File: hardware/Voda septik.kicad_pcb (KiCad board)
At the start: 2 copper layers, 1 part, among them U1 ESP32-DevKitC-30

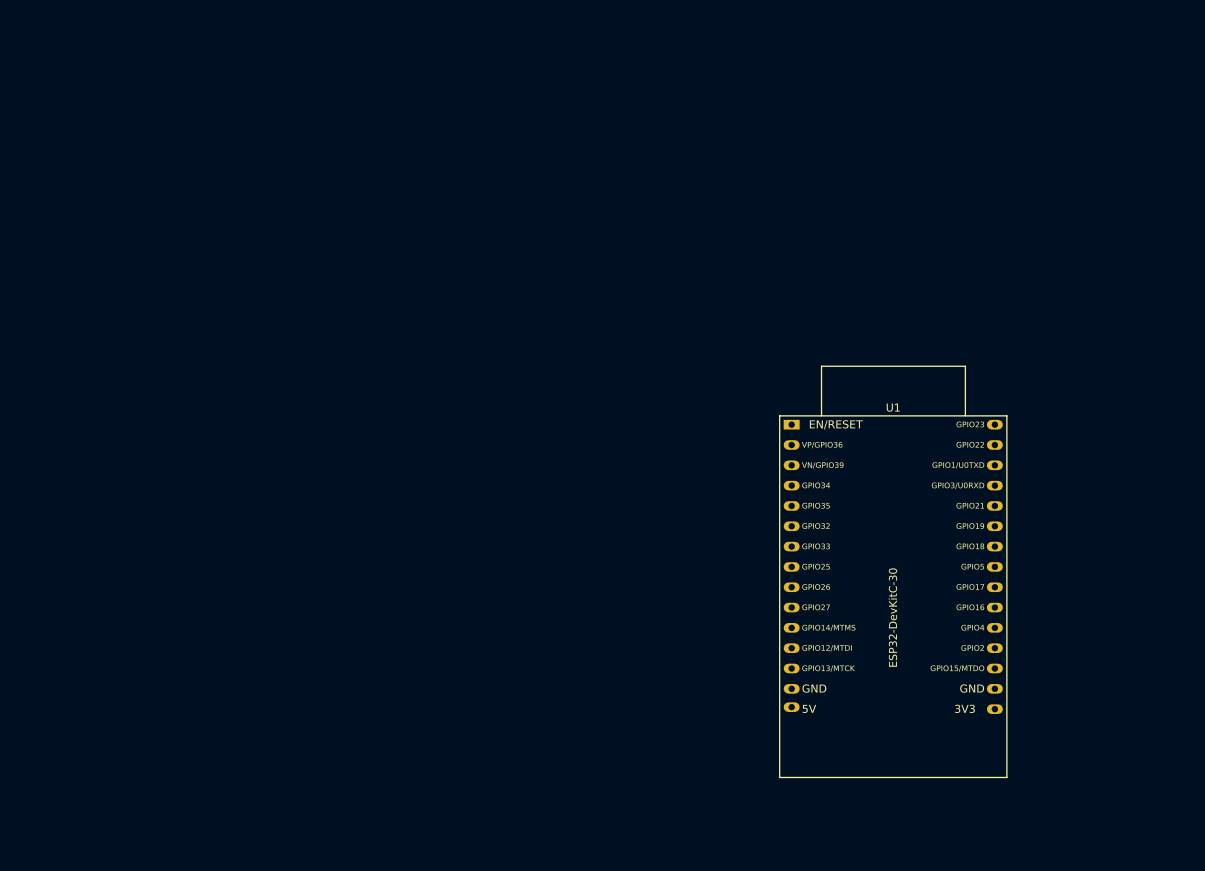
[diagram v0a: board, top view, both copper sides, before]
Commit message: Vyvéjíme PCB a jsme v v koncích díky malé krabičce.
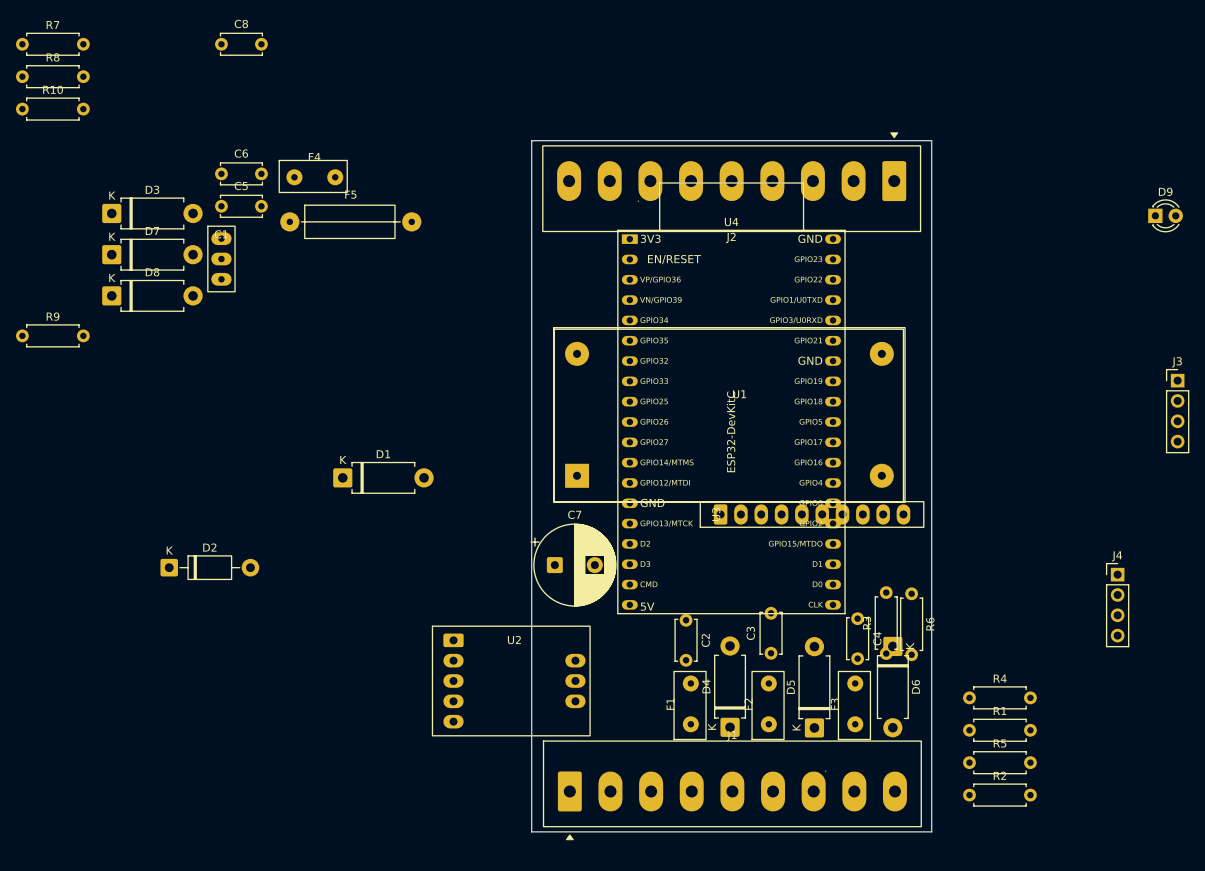
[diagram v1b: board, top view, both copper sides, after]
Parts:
- added C1: 100n, martin:Odruseni_3x_2.54mm, F.Cu at (53.2, 67.8)
- added C2: 100n, Capacitor_THT:C_Disc_D5.0mm_W2.5mm_P5.00mm, F.Cu at (111.3, 115.5)
- added C3: 100n, Capacitor_THT:C_Disc_D5.0mm_W2.5mm_P5.00mm, F.Cu at (121.9, 119.6)
- added C4: 100n, Capacitor_THT:C_Disc_D5.0mm_W2.5mm_P5.00mm, F.Cu at (132.7, 115.2)
- added C5: 1n, Capacitor_THT:C_Disc_D5.0mm_W2.5mm_P5.00mm, F.Cu at (53.2, 63.7)
- added C6: 100p, Capacitor_THT:C_Disc_D5.0mm_W2.5mm_P5.00mm, F.Cu at (53.2, 59.6)
- added C7: 470u, Capacitor_THT:CP_Radial_D10.0mm_P5.00mm, F.Cu at (94.9, 108.5)
- added C8: 100n, Capacitor_THT:C_Disc_D5.0mm_W2.5mm_P5.00mm, F.Cu at (53.2, 43.5)
- added D1: BZW04-5V8, Diode_THT:D_DO-15_P10.16mm_Horizontal, F.Cu at (68.4, 97.7)
- added D2: 1N4007, Diode_THT:D_DO-41_SOD81_P10.16mm_Horizontal, F.Cu at (46.7, 108.9)
- added D3: BZW06-26, Diode_THT:D_DO-15_P10.16mm_Horizontal, F.Cu at (39.5, 64.6)
- added D4: BZW04-5V8, Diode_THT:D_DO-15_P10.16mm_Horizontal, F.Cu at (116.8, 128.8)
- added D5: BZW04-5V8, Diode_THT:D_DO-15_P10.16mm_Horizontal, F.Cu at (127.3, 128.9)
- added D6: BZW04-5V8, Diode_THT:D_DO-15_P10.16mm_Horizontal, F.Cu at (137.1, 118.7)
- added D7: BZW04-5V8, Diode_THT:D_DO-15_P10.16mm_Horizontal, F.Cu at (39.5, 69.8)
- added D8: BZW04-5V8, Diode_THT:D_DO-15_P10.16mm_Horizontal, F.Cu at (39.5, 74.9)
- added D9: LED, LED_THT:LED_D3.0mm, F.Cu at (170.0, 64.9)
- added F1: 50mA, martin:Fuse_Disc_D8.3_W3.8_P5.1, F.Cu at (111.9, 128.4)
- added F2: 50mA, martin:Fuse_Disc_D8.3_W3.8_P5.1, F.Cu at (121.6, 128.4)
- added F3: 50mA, martin:Fuse_Disc_D8.3_W3.8_P5.1, F.Cu at (132.4, 128.4)
- added F4: 50mA, martin:Fuse_Disc_D8.3_W3.8_P5.1, F.Cu at (62.3, 60.1)
- added F5: 0,5A, martin:Fuse_Axial_L11mm_D3.9mm_P15.24mm_Horizontal, F.Cu at (61.8, 65.7)
- added J1: Screw_Terminal_01x09, martin:Svorky_EB147A_9_5.08, F.Cu at (96.8, 136.8)
- added J2: Screw_Terminal_01x09, martin:Svorky_EB147A_9_5.08, F.Cu at (137.3, 60.5)
- added J3: Display LCD I2C, Connector_PinHeader_2.54mm:PinHeader_1x04_P2.54mm_Vertical, F.Cu at (172.7, 85.5)
- added J4: Display TM1637, Connector_PinHeader_2.54mm:PinHeader_1x04_P2.54mm_Vertical, F.Cu at (165.2, 109.7)
- added R1: 100R, Resistor_THT:R_Axial_DIN0207_L6.3mm_D2.5mm_P7.62mm_Horizontal, F.Cu at (146.7, 129.2)
- added R10: 330R, Resistor_THT:R_Axial_DIN0207_L6.3mm_D2.5mm_P7.62mm_Horizontal, F.Cu at (28.3, 51.5)
- added R2: 100R, Resistor_THT:R_Axial_DIN0207_L6.3mm_D2.5mm_P7.62mm_Horizontal, F.Cu at (146.7, 137.3)
- added R3: 100R, Resistor_THT:R_Axial_DIN0207_L6.3mm_D2.5mm_P7.62mm_Horizontal, F.Cu at (136.3, 119.6)
- added R4: 2k2, Resistor_THT:R_Axial_DIN0207_L6.3mm_D2.5mm_P7.62mm_Horizontal, F.Cu at (146.7, 125.2)
- added R5: 2k2, Resistor_THT:R_Axial_DIN0207_L6.3mm_D2.5mm_P7.62mm_Horizontal, F.Cu at (146.7, 133.2)
- added R6: 2k2, Resistor_THT:R_Axial_DIN0207_L6.3mm_D2.5mm_P7.62mm_Horizontal, F.Cu at (139.5, 112.1)
- added R7: 2k2, Resistor_THT:R_Axial_DIN0207_L6.3mm_D2.5mm_P7.62mm_Horizontal, F.Cu at (28.3, 43.5)
- added R8: 3k9, Resistor_THT:R_Axial_DIN0207_L6.3mm_D2.5mm_P7.62mm_Horizontal, F.Cu at (28.3, 47.5)
- added R9: 56R, Resistor_THT:R_Axial_DIN0207_L6.3mm_D2.5mm_P7.62mm_Horizontal, F.Cu at (28.3, 79.9)
- added U1: DC-DC 24V -> 5V, martin:LM2596 DC-DC HW-411, F.Cu at (97.7, 97.4)
- added U2: MAX3485-modul, martin:MAX3485-modul, F.Cu at (82.2, 118.0)
- added U3: ADS1115IDGS, martin:ADS1115_modul, F.Cu at (115.6, 102.2)
- U4: renamed from U1; value ESP32-DevKitC-30 -> ESP32-DevKitC; footprint martin:ESP32-DevKitC-30 -> PCM_Espressif:ESP32-DevKitC
- moved U4 30.8 mm to (104.3, 67.8)
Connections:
- U4 pad 1: unconnected-(U1-CHIP_PU-Pad1) -> +3.3V
- U4 pad 10: unconnected-(U1-ADC2_CH7/GPIO27-Pad10) -> Net-(J3-SDA)
- U4 pad 14: unconnected-(U1-GND-Pad14) -> GND
- U4 pad 19: unconnected-(U1-ADC2_CH2/GPIO2-Pad19) -> +5V
- U4 pad 24: Net-(U1-GPIO18) -> unconnected-(U4-ADC2_CH2/GPIO2-Pad24)
- U4 pad 27: unconnected-(U1-U0RXD/GPIO3-Pad27) -> Net-(U2-RXD)
- U4 pad 28: unconnected-(U1-U0TXD/GPIO1-Pad28) -> Net-(U2-TXD)
- U4 pad 29: unconnected-(U1-GPIO22-Pad29) -> Net-(U2-EN)
- U4 pad 30: unconnected-(U1-GPIO23-Pad30) -> Net-(J4-CLK)
- U4 pad 7: unconnected-(U1-32K_XN/GPIO33/ADC1_CH5-Pad7) -> /průtok
- U4 pad 8: unconnected-(U1-DAC_1/ADC2_CH8/GPIO25-Pad8) -> /teploměry
- U4 pad 9: unconnected-(U1-DAC_2/ADC2_CH9/GPIO26-Pad9) -> Net-(J3-SCL)
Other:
- board outline added: 50 x 86.4 mm

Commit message: Tak už to mám všechno naroutováno
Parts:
- added U5: CA56-12CGKWA, martin:DISPLAY_clok_MOUNT_4xM3, F.Cu at (117.3, 86.3)
- D1, D3, D4, D5, D6, D7, D8: footprint Diode_THT:D_DO-15_P10.16mm_Horizontal -> Diode_THT:D_DO-15_P2.54mm_Vertical_AnodeUp
- D2: footprint Diode_THT:D_DO-41_SOD81_P10.16mm_Horizontal -> Diode_THT:D_DO-15_P2.54mm_Vertical_AnodeUp
- J1: value Screw_Terminal_01x09 -> Napájení a 4-20mA senzory; footprint martin:Svorky_EB147A_9_5.08 -> martin:Svorky_EB147A_8_5.08
- J2: footprint martin:Svorky_EB147A_9_5.08 -> martin:Svorky_EB147A_8_5.08
- R1, R10, R2, R3, R4, R5, R6, R7, R8, R9: footprint Resistor_THT:R_Axial_DIN0207_L6.3mm_D2.5mm_P7.62mm_Horizontal -> Resistor_THT:R_Axial_DIN0207_L6.3mm_D2.5mm_P2.54mm_Vertical
- U3: footprint martin:ADS1115_modul -> martin:ADS1115_modul_vertical
- moved R10 139.6 mm to (154.2, 111.8)
- moved R8 101.2 mm to (115.3, 99.4), turned to 90 degrees
- moved R7 96.4 mm to (120.3, 72.3), turned to 90 degrees
- moved C8 91.6 mm to (107.3, 117.3), turned to 180 degrees
- moved D3 89.4 mm to (103.2, 127.3), turned to 180 degrees
- moved R9 88.0 mm to (115.8, 70.3), turned to -90 degrees
- moved U2 87.3 mm to (153.8, 68.0), turned to 180 degrees
- moved D7 85.5 mm to (120.3, 97.9), turned to -90 degrees
- moved F4 77.9 mm to (120.6, 111.8), turned to 180 degrees
- moved D8 76.3 mm to (115.8, 76.9), turned to -90 degrees
- moved C5 72.9 mm to (120.3, 92.3), turned to 180 degrees
- moved C6 69.5 mm to (120.8, 75.8), turned to -90 degrees
- moved C1 67.3 mm to (98.8, 117.3), turned to -90 degrees
- moved F5 64.6 mm to (92.7, 122.3)
- moved D1 59.8 mm to (123.3, 121.3)
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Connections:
- C3 pad 1: /tlak_pred_filtrem -> Net-(U3-AIN2)
- J1 pad 3: unconnected-(J1-Pad3) -> Net-(J1-hladina_+24V)
- J1 pad 4: Net-(J1-hladina_+24V) -> Net-(D4-K)
- J1 pad 5: Net-(D4-K) -> Net-(J1-tlak_před_filtrem_+24V)
- J1 pad 6: Net-(J1-tlak_před_filtrem_+24V) -> Net-(D5-K)
- J1 pad 7: Net-(D5-K) -> Net-(J1-tlak_za_filtrem_+24V)
- J1 pad 8: Net-(J1-tlak_za_filtrem_+24V) -> Net-(D6-K)
- J2 pad 1: unconnected-(J2-Pad1) -> Net-(J2-A_RS485_elektroměr)
- J2 pad 2: GND -> Net-(J2-B_RS485_elektroměr)
- J2 pad 3: Net-(D8-K) -> GND
- J2 pad 4: Net-(J2-1wire+5V) -> Net-(D8-K)
- J2 pad 5: GND -> Net-(J2-1wire+5V)
- J2 pad 6: Net-(D7-K) -> GND
- J2 pad 7: Net-(J2-1wire+5V) -> Net-(D7-K)
- J2 pad 8: Net-(J2-B_RS485_elektroměr) -> Net-(J2-1wire+5V)
- R10 pad 1: Net-(U4-GPIO23) -> Net-(U4-GPIO16)
- R5 pad 1: /tlak_pred_filtrem -> Net-(U3-AIN2)
- U3 pad 1: GND -> +3.3V
- U3 pad 10: Net-(U3-SCL) -> /hladina 4-20mA
- U3 pad 2: unconnected-(U3-ALERT/RDY-Pad2) -> GND
- U3 pad 3: GND -> Net-(U3-SCL)
- U3 pad 4: /hladina 4-20mA -> Net-(U3-SDA)
- U3 pad 5: /tlak_pred_filtrem -> GND
- U3 pad 6: /tlak_za_filtrem -> unconnected-(U3-ALERT/RDY-Pad6)
- U3 pad 8: +3.3V -> /tlak_za_filtrem
- U3 pad 9: Net-(U3-SDA) -> Net-(U3-AIN2)
- U4 pad 10: Net-(J3-SDA) -> Net-(U2-RXD)
- U4 pad 11: unconnected-(U4-ADC2_CH7/GPIO27-Pad11) -> Net-(U2-TXD)
- U4 pad 12: unconnected-(U4-MTMS/GPIO14/ADC2_CH6-Pad12) -> Net-(U3-SDA)
- U4 pad 15: unconnected-(U4-MTCK/GPIO13/ADC2_CH4-Pad15) -> Net-(U3-SCL)
- U4 pad 16: unconnected-(U4-SD_DATA2/GPIO9-Pad16) -> (no net)
- U4 pad 17: unconnected-(U4-SD_DATA3/GPIO10-Pad17) -> (no net)
- U4 pad 18: unconnected-(U4-CMD-Pad18) -> (no net)
- U4 pad 20: unconnected-(U4-SD_CLK/GPIO6-Pad20) -> (no net)
- U4 pad 21: unconnected-(U4-SD_DATA0/GPIO7-Pad21) -> (no net)
- U4 pad 22: unconnected-(U4-SD_DATA1/GPIO8-Pad22) -> (no net)
- U4 pad 27: Net-(U2-RXD) -> Net-(U4-GPIO16)
- U4 pad 28: Net-(U2-TXD) -> Net-(J4-CLK)
- U4 pad 29: Net-(U2-EN) -> unconnected-(U4-GPIO5-Pad29)
- U4 pad 30: Net-(J4-CLK) -> Net-(J4-DIO)
- U4 pad 31: Net-(J4-DIO) -> unconnected-(U4-GPIO19-Pad31)
- U4 pad 33: Net-(U3-SCL) -> unconnected-(U4-GPIO21-Pad33)
- U4 pad 36: Net-(U3-SDA) -> Net-(J3-SDA)
- U4 pad 37: Net-(U4-GPIO23) -> Net-(J3-SCL)
- U4 pad 7: /průtok -> /teploměry
- U4 pad 8: /teploměry -> /průtok
- U4 pad 9: Net-(J3-SCL) -> Net-(U2-EN)
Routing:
- net GND: track 0.00 -> 444.0 mm, vias 0 -> 7
- net +5V: track 0.00 -> 149.2 mm, vias 0 -> 1
- net +3.3V: track 0.00 -> 141.5 mm, vias 0 -> 2
- net Net-(J2-1wire+5V): track 0.00 -> 81.6 mm
- net Net-(D7-K): track 0.00 -> 51.6 mm
- net Net-(D2-K): track 0.00 -> 51.5 mm
- net Net-(U2-EN): track 0.00 -> 50.3 mm
- net Net-(D4-K): track 0.00 -> 48.0 mm
- net Net-(U2-TXD): track 0.00 -> 45.5 mm
- net Net-(U2-RXD): track 0.00 -> 44.7 mm
- net Net-(D5-K): track 0.00 -> 40.9 mm
- net Net-(U3-SDA): track 0.00 -> 30.4 mm
- net /hladina 4-20mA: track 0.00 -> 29.8 mm
- net Net-(D8-K): track 0.00 -> 23.0 mm
- net Net-(U3-SCL): track 0.00 -> 21.6 mm
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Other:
- board size 50 x 86.4 mm -> 67.7 x 86.4 mm

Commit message: Hotový návrh desky a schématu, které jdou do výroby.
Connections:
- U4 pad 16: (no net) -> unconnected-(U4-SD_DATA2/GPIO9-Pad16)
- U4 pad 17: (no net) -> unconnected-(U4-SD_DATA3/GPIO10-Pad17)
- U4 pad 18: (no net) -> unconnected-(U4-CMD-Pad18)
- U4 pad 20: (no net) -> unconnected-(U4-SD_CLK/GPIO6-Pad20)
- U4 pad 21: (no net) -> unconnected-(U4-SD_DATA0/GPIO7-Pad21)
- U4 pad 22: (no net) -> unconnected-(U4-SD_DATA1/GPIO8-Pad22)
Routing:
- net GND: track 444.0 -> 20.6 mm
- net +3.3V: track 141.5 -> 157.3 mm, vias 2 -> 3
- net +5V: track 149.2 -> 151.6 mm, vias 1 -> 2
- added copper zone on B.Cu, net GND
- added copper zone on F.Cu, net GND
